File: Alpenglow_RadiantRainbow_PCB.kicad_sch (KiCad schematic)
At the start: 17 parts, among them SW1 SW_SPDT

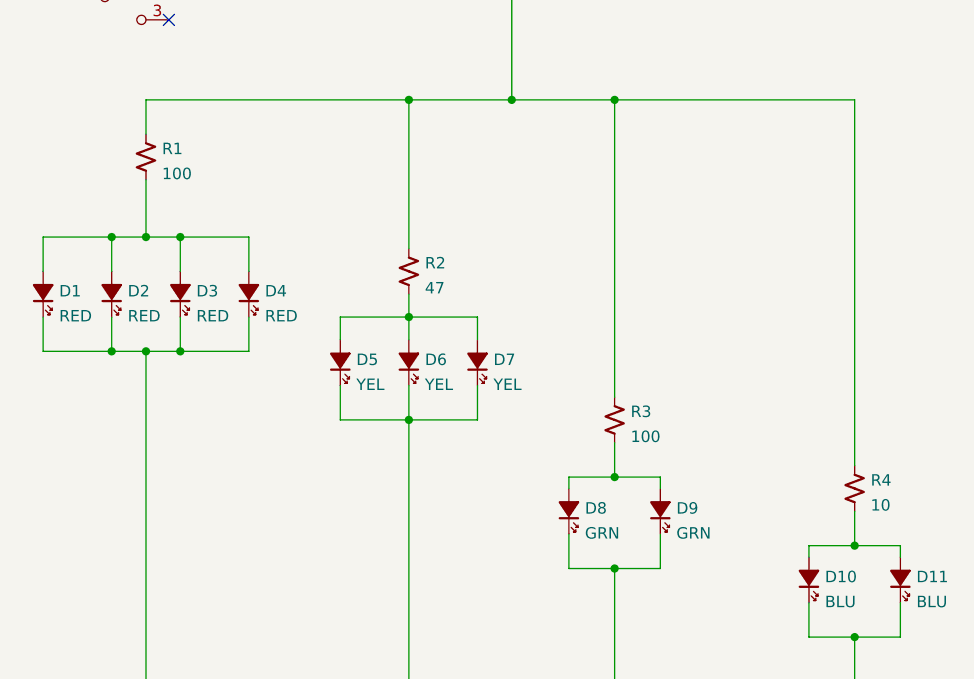
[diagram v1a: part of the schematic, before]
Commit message: Updated resistor values.  Cleaned up foot print library.
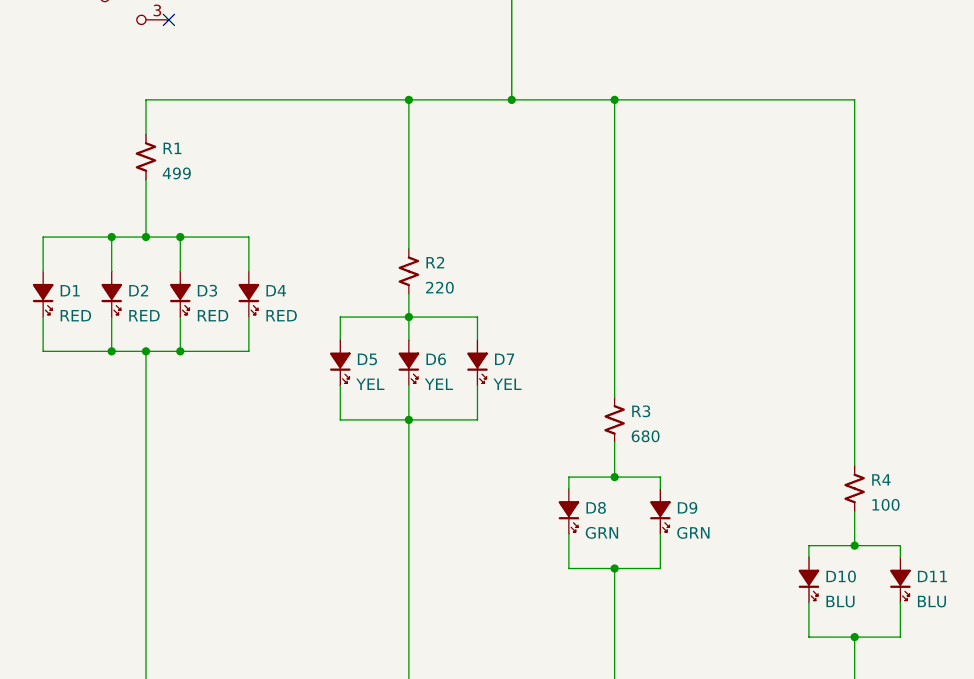
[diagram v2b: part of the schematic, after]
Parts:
- R1: value 100 -> 499
- R2: value 47 -> 220
- R3: value 100 -> 680
- R4: value 10 -> 100
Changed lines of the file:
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@@
       (effects (font (size 1.27 1.27)) (justify left))
     )
-    (property "Value" "100" (id 1) (at 145.288 70.4466 0)
+    (property "Value" "499" (id 1) (at 145.288 70.4466 0)
       (effects (font (size 1.27 1.27)) (justify left))
     )
@@
       (effects (font (size 1.27 1.27)) (justify left))
     )
-    (property "Value" "47" (id 1) (at 174.498 83.1466 0)
+    (property "Value" "220" (id 1) (at 174.498 83.1466 0)
       (effects (font (size 1.27 1.27)) (justify left))
     )
@@
       (effects (font (size 1.27 1.27)) (justify left))
     )
-    (property "Value" "100" (id 1) (at 197.358 99.6566 0)
+    (property "Value" "680" (id 1) (at 197.358 99.6566 0)
       (effects (font (size 1.27 1.27)) (justify left))
     )
@@
       (effects (font (size 1.27 1.27)) (justify left))
     )
-    (property "Value" "10" (id 1) (at 224.028 107.2766 0)
+    (property "Value" "100" (id 1) (at 224.028 107.2766 0)
       (effects (font (size 1.27 1.27)) (justify left))
     )
@@
     )
     (path "/162bcbf8-fe68-4c54-95da-92be290dc035"
-      (reference "R1") (unit 1) (value "100") (footprint "Resistor_THT:R_Axial_DIN0207_L6.3mm_D2.5mm_P10.16mm_Horizontal")
+      (reference "R1") (unit 1) (value "499") (footprint "Resistor_THT:R_Axial_DIN0207_L6.3mm_D2.5mm_P10.16mm_Horizontal")
     )
     (path "/9096053c-3ff1-40be-a240-911e6956b077"
-      (reference "R2") (unit 1) (value "47") (footprint "Resistor_THT:R_Axial_DIN0207_L6.3mm_D2.5mm_P10.16mm_Horizontal")
+      (reference "R2") (unit 1) (value "220") (footprint "Resistor_THT:R_Axial_DIN0207_L6.3mm_D2.5mm_P10.16mm_Horizontal")
     )
     (path "/f255e250-fb9b-4243-b58b-08fa425a1b1f"
-      (reference "R3") (unit 1) (value "100") (footprint "Resistor_THT:R_Axial_DIN0207_L6.3mm_D2.5mm_P10.16mm_Horizontal")
+      (reference "R3") (unit 1) (value "680") (footprint "Resistor_THT:R_Axial_DIN0207_L6.3mm_D2.5mm_P10.16mm_Horizontal")
     )
     (path "/f7ce14aa-bddc-4eee-aade-793f191990a0"
-      (reference "R4") (unit 1) (value "10") (footprint "Resistor_THT:R_Axial_DIN0207_L6.3mm_D2.5mm_P10.16mm_Horizontal")
+      (reference "R4") (unit 1) (value "100") (footprint "Resistor_THT:R_Axial_DIN0207_L6.3mm_D2.5mm_P10.16mm_Horizontal")
     )
     (path "/e5ece5da-4299-41c5-906b-9289c206bf0d"

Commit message: Updated schematic, Kept mounting pins connected to GND to have the b.cu connected
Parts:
- SW1: footprint Alpenglow:SW_SLIDE_RTA -> Alpenglow:SW_SPDT_SLIDE_THRU_RTA
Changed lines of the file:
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@@
     (property "Reference" "SW1" (id 0) (at 140.97 43.9125 0))
     (property "Value" "SW_SPDT" (id 1) (at 140.97 46.6876 0))
-    (property "Footprint" "Alpenglow:SW_SLIDE_RTA" (id 2) (at 140.97 50.8 0)
+    (property "Footprint" "Alpenglow:SW_SPDT_SLIDE_THRU_RTA" (id 2) (at 140.97 50.8 0)
       (effects (font (size 1.27 1.27)) hide)
     )
@@
     )
     (path "/e5ece5da-4299-41c5-906b-9289c206bf0d"
-      (reference "SW1") (unit 1) (value "SW_SPDT") (footprint "Alpenglow:SW_SLIDE_RTA")
+      (reference "SW1") (unit 1) (value "SW_SPDT") (footprint "Alpenglow:SW_SPDT_SLIDE_THRU_RTA")
     )
   )

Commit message: Updated Switch, Removed GND pour and added GND traces, Updated artwork
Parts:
- SW1: footprint Alpenglow:SW_SPDT_SLIDE_THRU_RTA -> Alpenglow:Alpenglow_SW_SPDT_3pin_RTA
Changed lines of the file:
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@@
     (property "Reference" "SW1" (id 0) (at 140.97 43.9125 0))
     (property "Value" "SW_SPDT" (id 1) (at 140.97 46.6876 0))
-    (property "Footprint" "Alpenglow:SW_SPDT_SLIDE_THRU_RTA" (id 2) (at 140.97 50.8 0)
+    (property "Footprint" "Alpenglow:Alpenglow_SW_SPDT_3pin_RTA" (id 2) (at 140.97 50.8 0)
       (effects (font (size 1.27 1.27)) hide)
     )
@@
     )
     (path "/e5ece5da-4299-41c5-906b-9289c206bf0d"
-      (reference "SW1") (unit 1) (value "SW_SPDT") (footprint "Alpenglow:SW_SPDT_SLIDE_THRU_RTA")
+      (reference "SW1") (unit 1) (value "SW_SPDT") (footprint "Alpenglow:Alpenglow_SW_SPDT_3pin_RTA")
     )
   )
